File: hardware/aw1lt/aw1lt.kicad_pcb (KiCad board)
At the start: 2 copper layers, 30 x 22 mm, 27 parts, among them J1 ISP, J2 FTDI Basic, Q1 PMOS_2.5A/30V, SW1 SW_Push, SW2 SW_Push, SW3 SW_Push, U1 DS3231MZ, U2 ATMEGA328P-AU

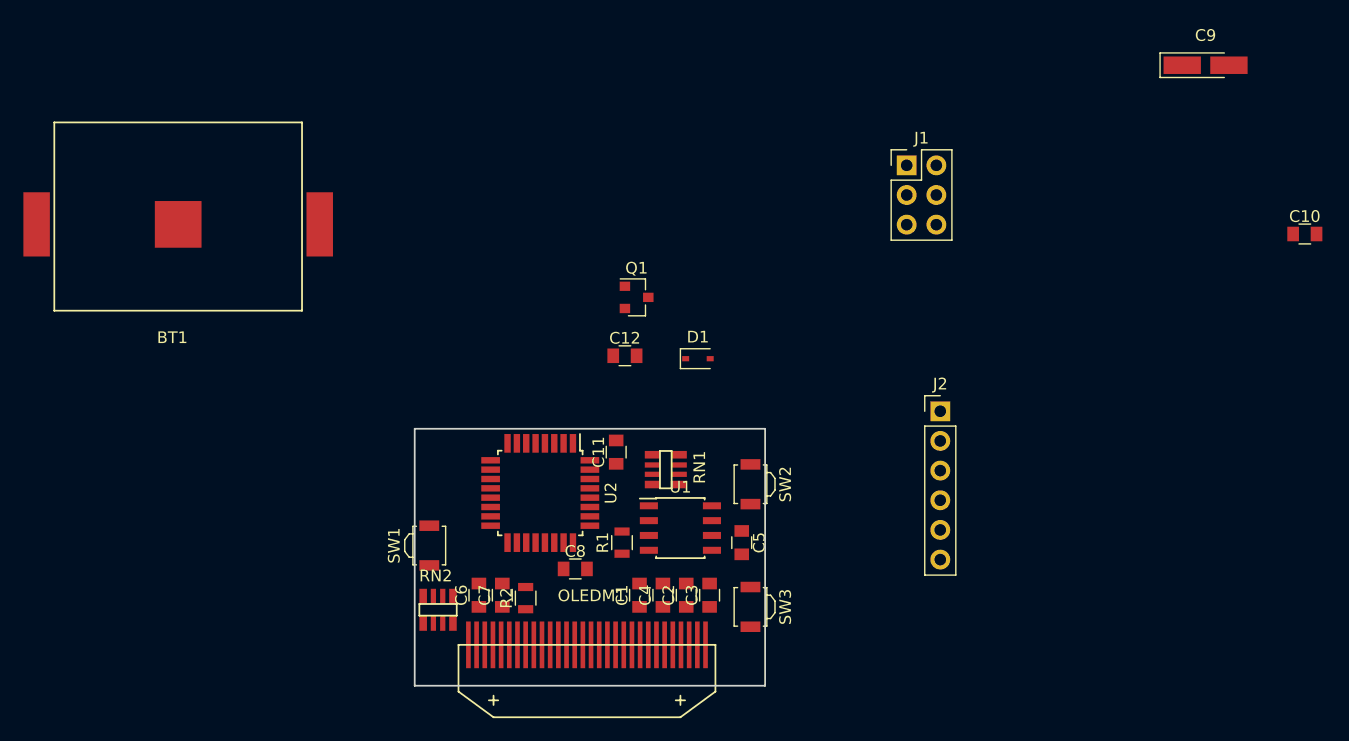
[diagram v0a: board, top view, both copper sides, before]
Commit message: have a better connector put down for the ISP and FTDI pins. considering removing the power switching circuit and not connecting the vcc of those pins
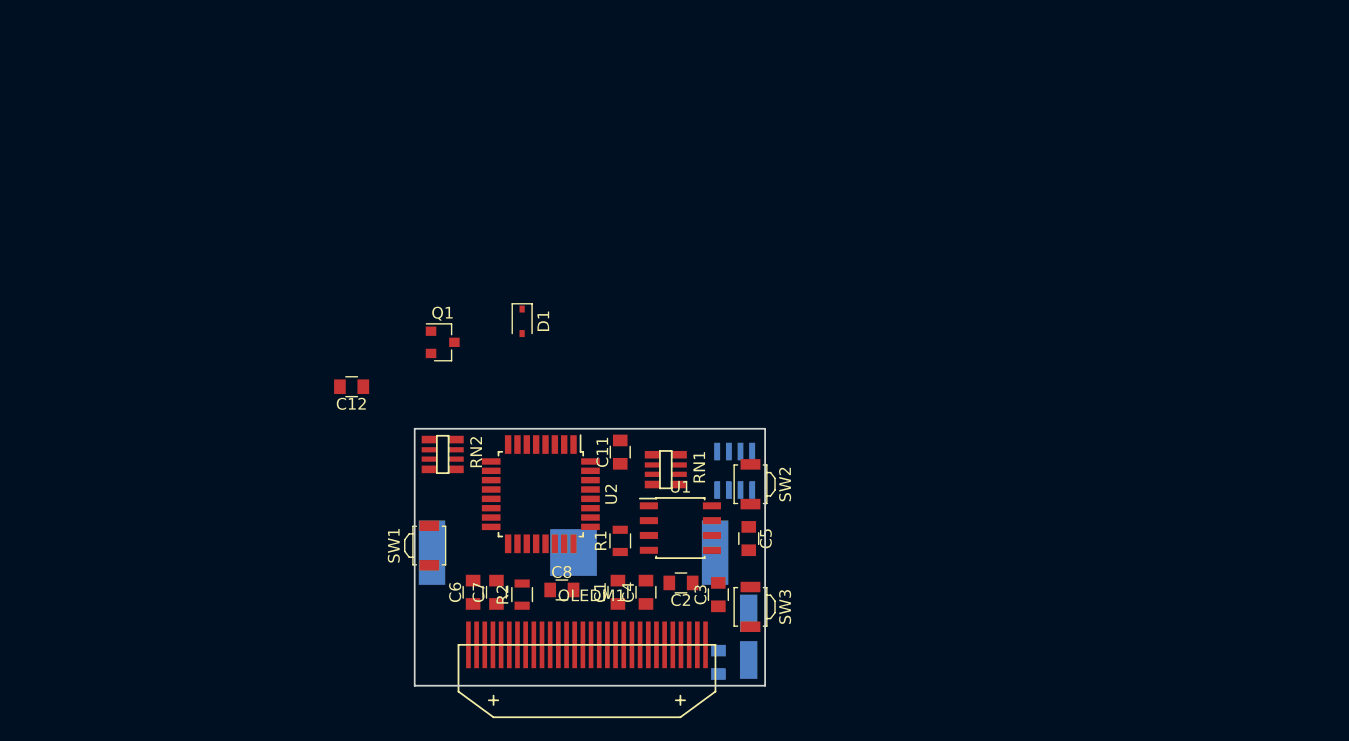
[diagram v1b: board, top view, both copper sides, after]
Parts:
- removed J2: FTDI Basic, Pin_Headers:Pin_Header_Straight_1x06_Pitch2.54mm
- BT1, C10, C9: moved to B.Cu
- J1: value ISP -> ISP_FTDI; footprint Pin_Headers:Pin_Header_Straight_2x03_Pitch2.54mm -> Pin_Headers:Pin_Header_Straight_2x04_Pitch1.00mm_SMD; moved to B.Cu
- moved C9 62.6 mm to (153.6, 142.8), turned to 270 degrees
- moved C10 62.2 mm to (151.0, 145.0), turned to 270 degrees
- moved BT1 44.0 mm to (138.6, 135.6)
- moved J1 30.0 mm to (152.4, 128.6), turned to 270 degrees
- moved C12 23.5 mm to (119.6, 121.4), turned to 180 degrees
- moved Q1 17.0 mm to (127.4, 117.6)
- moved D1 15.4 mm to (134.2, 115.8), turned to 270 degrees
- moved RN2 13.3 mm to (127.4, 127.2), turned to 90 degrees
- moved C8 2.14 mm to (137.6, 138.8)
- moved C1 1.87 mm to (142.4, 139.0)
- moved C4 1.47 mm to (144.8, 139.0)
- moved C2 1.14 mm to (147.8, 138.2), turned to 180 degrees
- moved C3 0.75 mm to (151.0, 139.2)
- moved C5 0.69 mm to (153.6, 134.4)
- moved C6 0.56 mm to (130.0, 139.0)
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
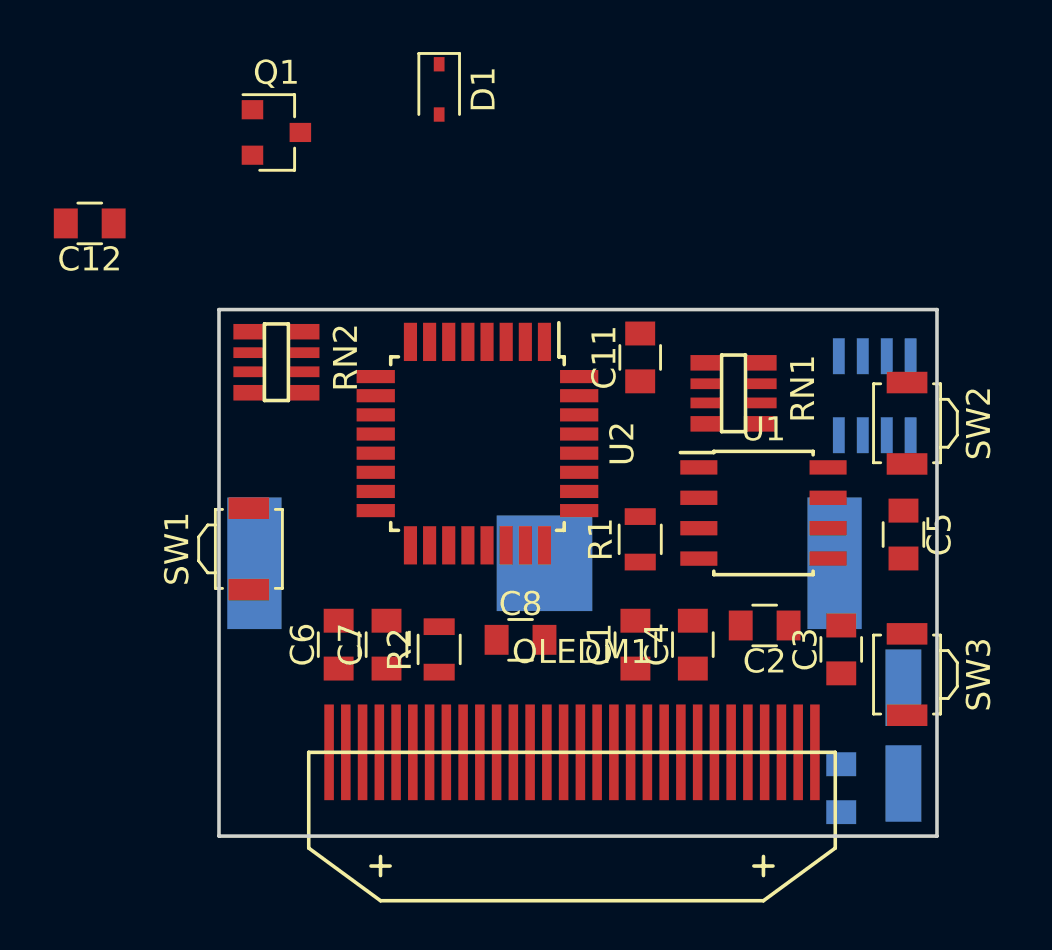
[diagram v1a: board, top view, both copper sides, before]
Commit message: adding in a speaker, getting things fitting in the pcb
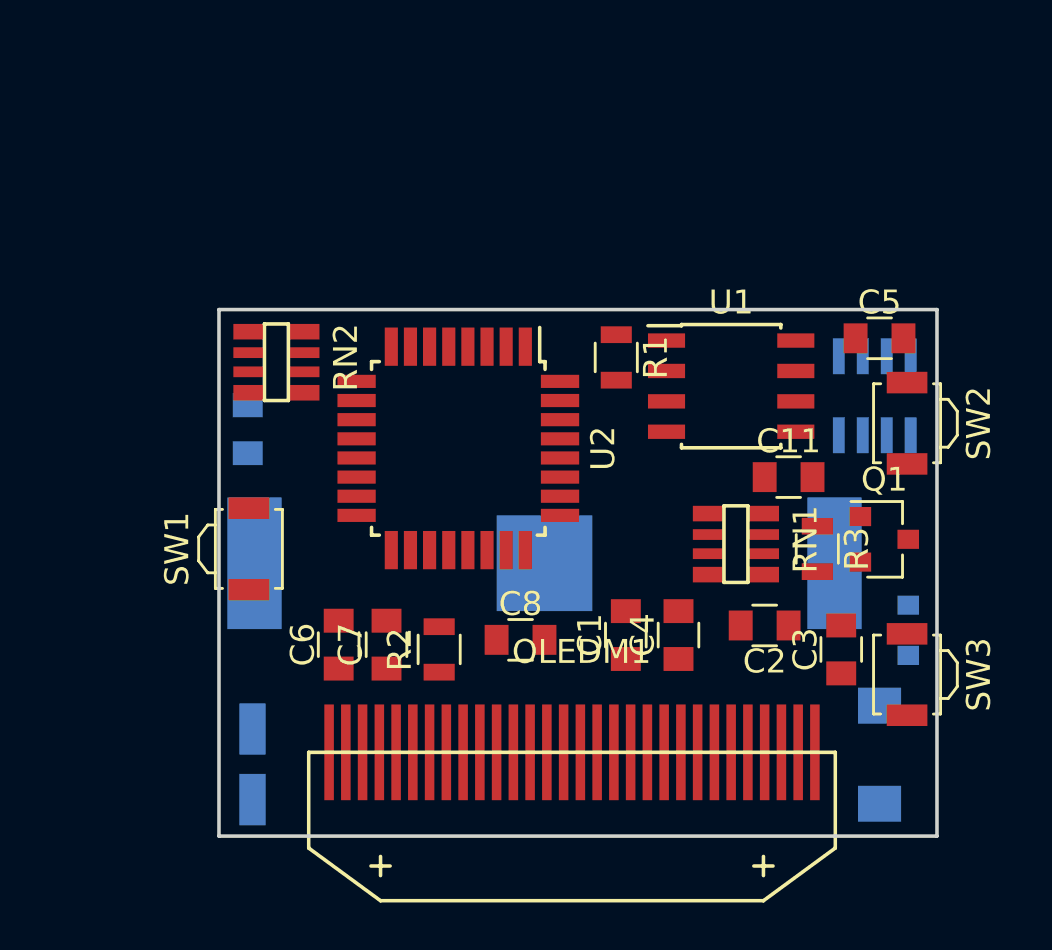
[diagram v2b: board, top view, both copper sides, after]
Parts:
- removed C12: 1uF, Capacitors_SMD:C_0805
- added BZ1: Buzzer, aw-1:Buzzer_ST-0402S, B.Cu at (152.6, 143.6)
- added R3: 180, Resistors_SMD:R_0805, F.Cu at (150.0, 135.0)
- C9: footprint Capacitors_Tantalum_SMD:CP_Tantalum_Case-A_EIA-3216-18_Hand -> Capacitors_Tantalum_SMD:CP_Tantalum_Case-A_EIA-3216-18_Wave
- D1: value BAT20J -> D; footprint Diodes_SMD:D_SOD-323 -> Diodes_SMD:D_0805; moved to B.Cu
- Q1: value PMOS_2.5A/30V -> BSS138
- moved Q1 30.6 mm to (152.8, 134.6)
- moved D1 29.9 mm to (153.8, 138.4)
- moved C10 29.0 mm to (126.2, 130.0)
- moved C9 27.2 mm to (126.4, 144.0)
- moved C5 8.26 mm to (152.6, 126.2), turned to 0 degrees
- moved C11 7.96 mm to (148.8, 132.0), turned to 0 degrees
- moved R1 7.67 mm to (141.6, 127.0), turned to 270 degrees
- moved RN1 6.30 mm to (146.6, 134.8)
- moved U1 5.47 mm to (146.4, 128.2)
- moved U2 0.82 mm to (135.0, 130.8)
- moved C4 0.72 mm to (144.2, 138.6)
- moved C1 0.57 mm to (142.0, 138.6)
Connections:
- D1 pad 1: VCC -> +3V3
- D1 pad 2: +5V -> Net-(BZ1-Pad2)
- J1 pad 2: VCC -> +3V3
- Q1 pad 1: +3V3 -> Net-(Q1-Pad1)
- Q1 pad 2: +5V -> GND
- Q1 pad 3: VCC -> Net-(BZ1-Pad2)
- RN1 pad 1: VCC -> +3V3
- RN1 pad 2: VCC -> +3V3
- RN1 pad 3: VCC -> +3V3
- RN1 pad 4: +5V -> (no net)
- RN1 pad 5: GND -> (no net)
- U2 pad 18: VCC -> +3V3
- U2 pad 23: VIB -> SPKR
- U2 pad 4: VCC -> +3V3
- U2 pad 6: VCC -> +3V3

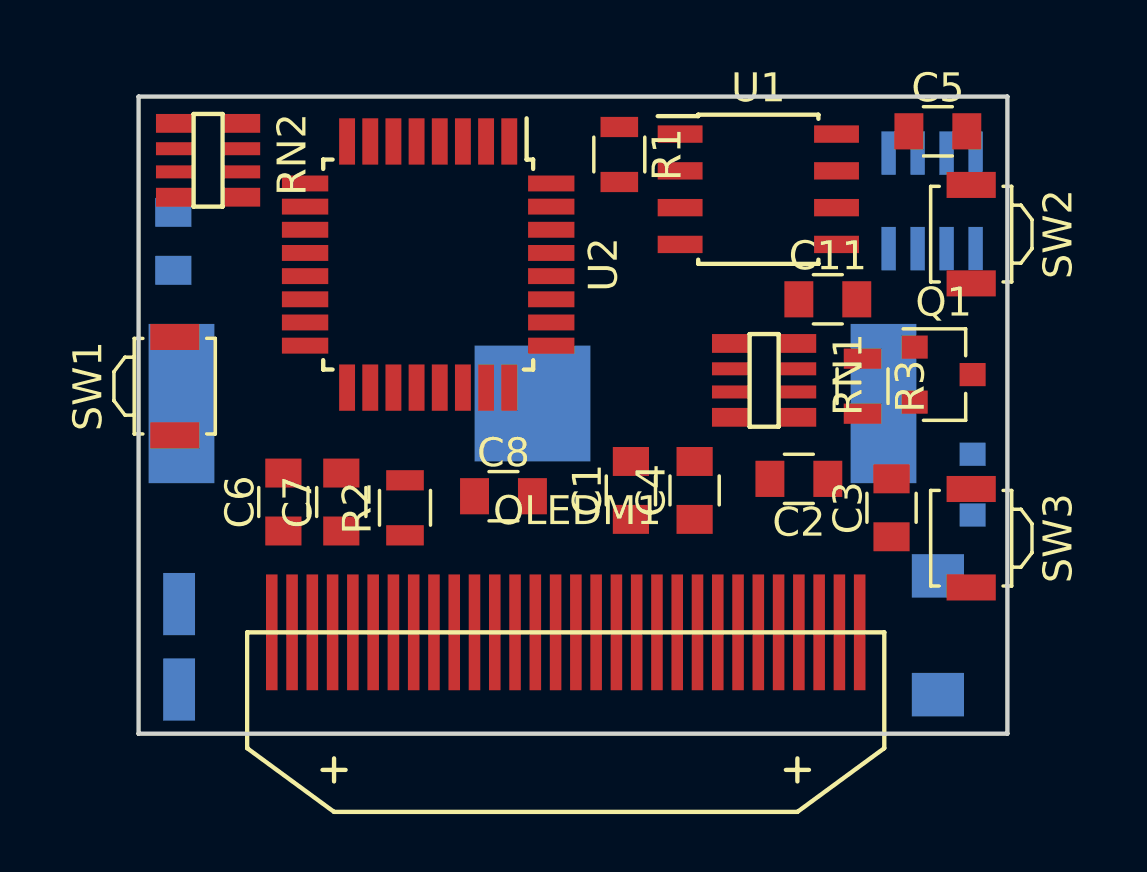
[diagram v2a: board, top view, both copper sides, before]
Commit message: additional work on the pcb, realized that the buttons can be inline with the circuit board and a case attachment can be used to push the buttons
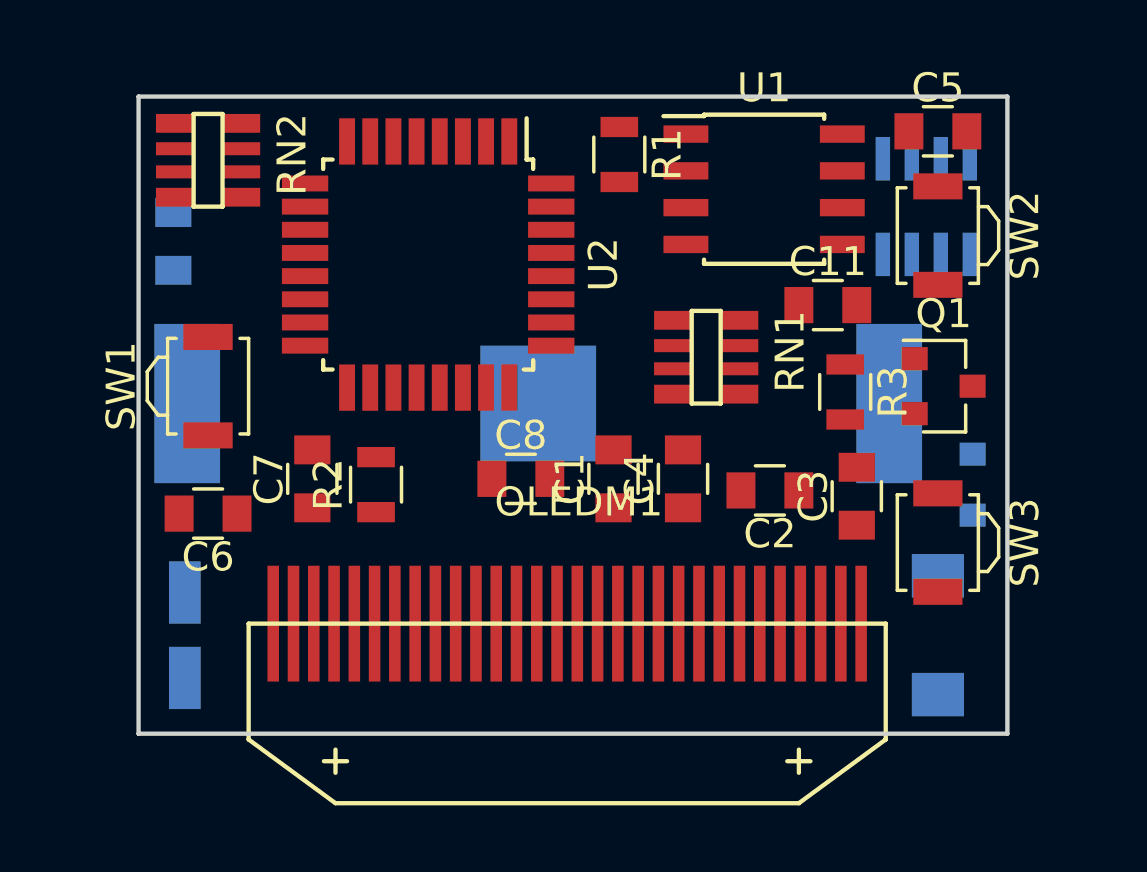
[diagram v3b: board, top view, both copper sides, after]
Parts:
- moved C6 2.63 mm to (127.4, 139.4), turned to 180 degrees
- moved RN1 2.15 mm to (144.6, 134.0)
- moved C7 1.28 mm to (131.0, 138.2)
- moved R2 1.28 mm to (133.2, 138.4)
- moved C3 1.26 mm to (149.8, 138.8)
- moved SW3 1.16 mm to (152.6, 140.4)
- moved SW2 1.15 mm to (152.6, 129.8)
- moved SW1 1.15 mm to (127.4, 135.0)
- moved C2 1.08 mm to (146.8, 138.6)
- moved C8 0.85 mm to (138.2, 138.2)
- moved C1 0.72 mm to (141.4, 138.2)
- moved R3 0.63 mm to (149.4, 135.2)
- moved C4 0.57 mm to (143.8, 138.2)
- moved C9 0.45 mm to (126.6, 143.6)
- moved Q1 0.40 mm to (152.8, 135.0)
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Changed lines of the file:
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@@
   )
   (module Capacitors_SMD:C_0805 (layer F.Cu)
-    (at 142 138.6 90)
+    (at 141.4 138.2 90)
     (descr "Capacitor SMD 0805, reflow soldering, AVX (see smccp.pdf)")
     (tags "capacitor 0805")
@@
   )
   (module Capacitors_SMD:C_0805 (layer F.Cu)
-    (at 147.8 138.2 180)
+    (at 146.8 138.6 180)
     (descr "Capacitor SMD 0805, reflow soldering, AVX (see smccp.pdf)")
     (tags "capacitor 0805")
@@
   )
   (module Capacitors_SMD:C_0805 (layer F.Cu)
-    (at 151 139.2 90)
+    (at 149.8 138.8 90)
     (descr "Capacitor SMD 0805, reflow soldering, AVX (see smccp.pdf)")
     (tags "capacitor 0805")
@@
   )
   (module Capacitors_SMD:C_0805 (layer F.Cu)
-    (at 144.2 138.6 90)
+    (at 143.8 138.2 90)
     (descr "Capacitor SMD 0805, reflow soldering, AVX (see smccp.pdf)")
     (tags "capacitor 0805")
@@
   )
   (module Capacitors_SMD:C_0805 (layer F.Cu)
-    (at 130 139 90)
+    (at 127.4 139.4 180)
     (descr "Capacitor SMD 0805, reflow soldering, AVX (see smccp.pdf)")
     (tags "capacitor 0805")
     (attr smd)
-    (fp_text reference C6 (at 0 -1.5 90) (layer F.SilkS)
-      (effects (font (size 1 1) (thickness 0.15)))
-    )
-    (fp_text value 2.2uF (at 0 1.75 90) (layer F.Fab)
-      (effects (font (size 1 1) (thickness 0.15)))
-    )
-    (fp_text user %R (at 0 -1.5 90) (layer F.Fab)
+    (fp_text reference C6 (at 0 -1.5 180) (layer F.SilkS)
+      (effects (font (size 1 1) (thickness 0.15)))
+    )
+    (fp_text value 2.2uF (at 0 1.75 180) (layer F.Fab)
+      (effects (font (size 1 1) (thickness 0.15)))
+    )
+    (fp_text user %R (at 0 -1.5 180) (layer F.Fab)
       (effects (font (size 1 1) (thickness 0.15)))
     )
@@
     (fp_line (start 1.75 0.87) (end 1.75 -0.88) (layer F.CrtYd) (width 0.05))
     (fp_line (start 1.75 0.87) (end -1.75 0.87) (layer F.CrtYd) (width 0.05))
-    (pad 1 smd rect (at -1 0 90) (size 1 1.25) (layers F.Cu F.Paste F.Mask)
+    (pad 1 smd rect (at -1 0 180) (size 1 1.25) (layers F.Cu F.Paste F.Mask)
       (net 7 "Net-(C6-Pad1)"))
-    (pad 2 smd rect (at 1 0 90) (size 1 1.25) (layers F.Cu F.Paste F.Mask)
+    (pad 2 smd rect (at 1 0 180) (size 1 1.25) (layers F.Cu F.Paste F.Mask)
       (net 2 GND))
     (model Capacitors_SMD.3dshapes/C_0805.wrl
@@
   )
   (module Capacitors_SMD:C_0805 (layer F.Cu)
-    (at 132 139 90)
+    (at 131 138.2 90)
     (descr "Capacitor SMD 0805, reflow soldering, AVX (see smccp.pdf)")
     (tags "capacitor 0805")
@@
   )
   (module Capacitors_SMD:C_0805 (layer F.Cu)
-    (at 137.6 138.8)
+    (at 138.2 138.2)
     (descr "Capacitor SMD 0805, reflow soldering, AVX (see smccp.pdf)")
     (tags "capacitor 0805")
@@
   )
   (module Capacitors_SMD:C_0805 (layer F.Cu)
-    (at 148.8 132)
+    (at 148.8 132.2)
     (descr "Capacitor SMD 0805, reflow soldering, AVX (see smccp.pdf)")
     (tags "capacitor 0805")
@@
   )
   (module aw-1:SSD1306-FPC (layer F.Cu)
-    (at 139.75 143.5 180)
+    (at 139.8 143.2 180)
     (fp_text reference OLEDM1 (at -0.4 4.2 180) (layer F.SilkS)
       (effects (font (size 1 1) (thickness 0.15)))
@@
   )
   (module TO_SOT_Packages_SMD:SOT-23 (layer F.Cu)
-    (at 152.8 134.6)
+    (at 152.8 135)
     (descr "SOT-23, Standard")
     (tags SOT-23)
@@
   )
   (module Resistors_SMD:R_0805 (layer F.Cu)
-    (at 134.2 139.2 90)
+    (at 133.2 138.4 90)
     (descr "Resistor SMD 0805, reflow soldering, Vishay (see dcrcw.pdf)")
     (tags "resistor 0805")
@@
   )
   (module Buttons_Switches_SMD:SW_SPST_B3U-3000P (layer F.Cu)
-    (at 126.25 135 90)
+    (at 127.4 135 90)
     (descr "Ultra-small-sized Tactile Switch with High Contact Reliability, Side-actuated Model, without Ground Terminal, without Boss")
     (tags "Tactile Switch")
@@
   )
   (module Buttons_Switches_SMD:SW_SPST_B3U-3000P (layer F.Cu)
-    (at 153.75 129.75 270)
+    (at 152.6 129.8 270)
     (descr "Ultra-small-sized Tactile Switch with High Contact Reliability, Side-actuated Model, without Ground Terminal, without Boss")
     (tags "Tactile Switch")
@@
   )
   (module Buttons_Switches_SMD:SW_SPST_B3U-3000P (layer F.Cu)
-    (at 153.75 140.25 270)
+    (at 152.6 140.4 270)
     (descr "Ultra-small-sized Tactile Switch with High Contact Reliability, Side-actuated Model, without Ground Terminal, without Boss")
     (tags "Tactile Switch")
@@
   )
   (module Housings_SOIC:SOIC-8_3.9x4.9mm_Pitch1.27mm (layer F.Cu)
-    (at 146.4 128.2)
+    (at 146.6 128.2)
     (descr "8-Lead Plastic Small Outline (SN) - Narrow, 3.90 mm Body [SOIC] (see Microchip Packaging Specification 00000049BS.pdf)")
     (tags "SOIC 1.27")
@@
   )
   (module aw-1:EXB38V (layer F.Cu)
-    (at 146.6 134.8 90)
+    (at 144.6 134 90)
     (fp_text reference RN1 (at 0.2 2.9 90) (layer F.SilkS)
       (effects (font (size 1 1) (thickness 0.15)))
@@
   )
   (module aw-1:Coin_Cell_Retainer_3034 (layer B.Cu)
-    (at 138.6 135.6)
+    (at 138.8 135.6)
     (fp_text reference BT1 (at -0.5 -9.7) (layer B.SilkS)
       (effects (font (size 1 1) (thickness 0.15)) (justify mirror))
@@
   )
   (module Pin_Headers:Pin_Header_Straight_2x04_Pitch1.00mm_SMD (layer B.Cu)
-    (at 152.4 128.6 270)
+    (at 152.2 128.8 270)
     (descr "surface-mounted straight pin header, 2x04, 1.00mm pitch, double rows")
     (tags "Surface mounted pin header SMD 2x04 1.00mm double row")
@@
   )
   (module Capacitors_Tantalum_SMD:CP_Tantalum_Case-A_EIA-3216-18_Wave (layer B.Cu)
-    (at 126.4 144 270)
+    (at 126.6 143.6 270)
     (descr "Tantalum capacitor, Case A, EIA 3216-18, 3.2x1.6x1.6mm, Wave soldering footprint")
     (tags "capacitor tantalum smd")
@@
   )
   (module Resistors_SMD:R_0805 (layer F.Cu)
-    (at 150 135 270)
+    (at 149.4 135.2 270)
     (descr "Resistor SMD 0805, reflow soldering, Vishay (see dcrcw.pdf)")
     (tags "resistor 0805")

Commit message: starting to set tracks down
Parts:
- Q1: value BSS138 -> Q_NPN_CBE
- moved C1 3.61 mm to (141.6, 134.6)
- moved R3 1.81 mm to (147.6, 135.0)
- moved C3 1.80 mm to (149.8, 137.0)
- moved OLEDM1 1.80 mm to (139.8, 141.4)
- moved R2 1.61 mm to (134.6, 137.6), turned to 0 degrees
- moved C4 1.46 mm to (142.4, 137.8), turned to 0 degrees
- moved RN2 1.20 mm to (127.4, 128.4)
- moved C2 1.00 mm to (146.2, 137.8)
- moved C6 0.82 mm to (127.2, 138.6)
- moved C7 0.60 mm to (131.0, 137.6), turned to 180 degrees
- moved Q1 0.60 mm to (152.8, 134.4)
- moved RN1 0.60 mm to (144.6, 134.6), turned to 0 degrees
- moved C8 0.40 mm to (138.2, 137.8)
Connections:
- Q1 pad 1: Net-(Q1-Pad1) -> Net-(BZ1-Pad2)
- Q1 pad 2: GND -> Net-(Q1-Pad2)
- Q1 pad 3: Net-(BZ1-Pad2) -> GND
- R3 pad 1: Net-(Q1-Pad1) -> Net-(Q1-Pad2)
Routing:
- net SCL: track 0.00 -> 13.7 mm
- net PB0: track 0.00 -> 13.5 mm
- net SDA: track 0.00 -> 13.1 mm
- net INT0: track 0.00 -> 5.00 mm
- net PB2: track 0.00 -> 2.23 mm
- net PB1: track 0.00 -> 2.20 mm
